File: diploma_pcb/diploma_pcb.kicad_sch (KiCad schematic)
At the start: 22 parts, among them Q1 2SC3356, Q3 2SC3356

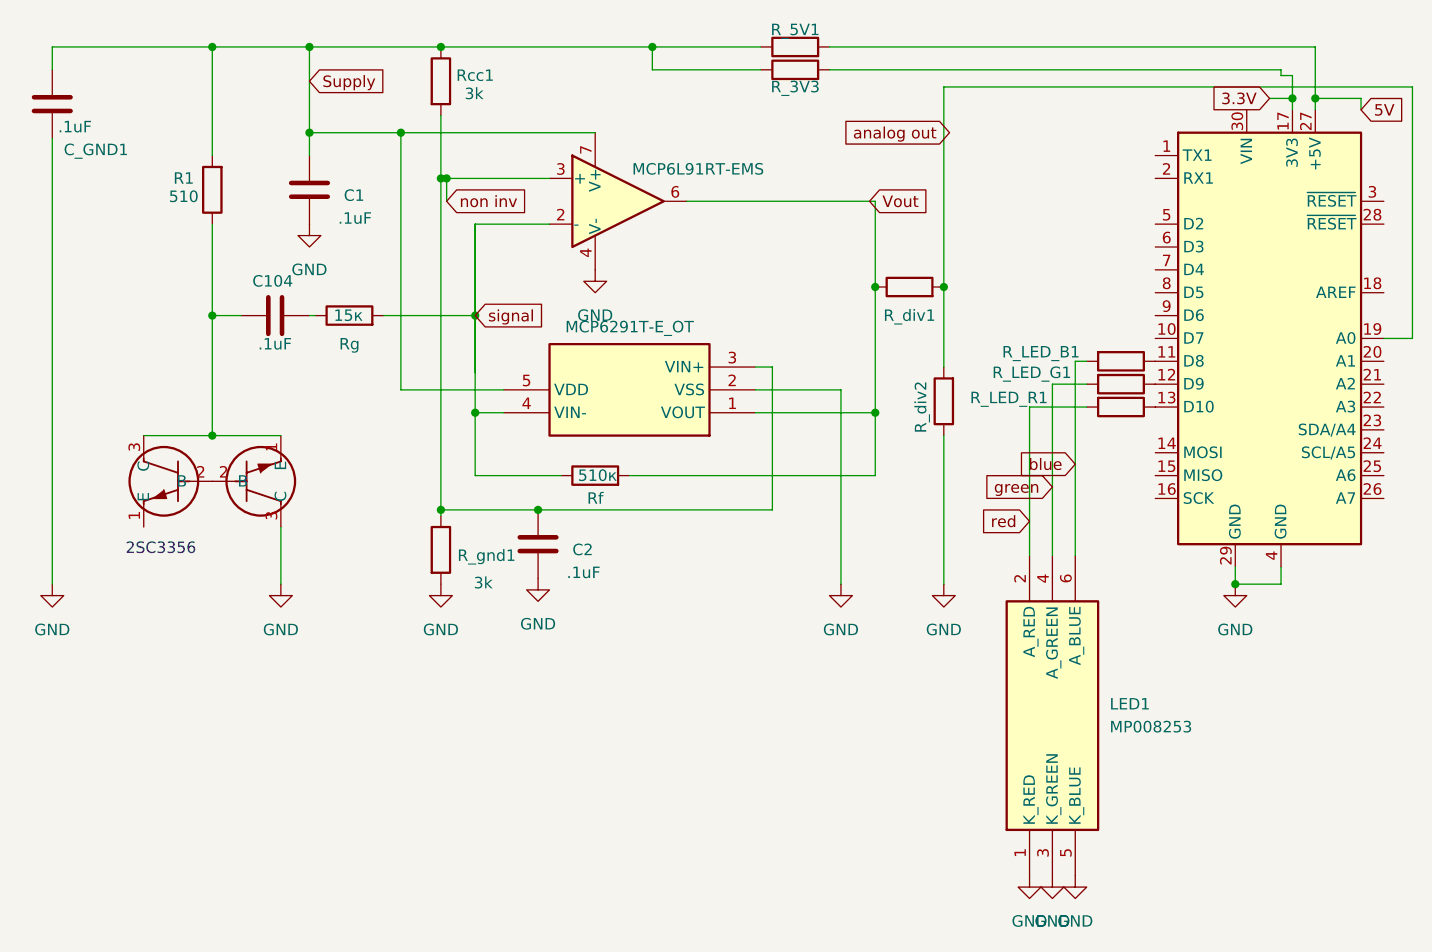
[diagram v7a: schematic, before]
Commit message: PCB added cap, larger pads, partialy fixed footprints
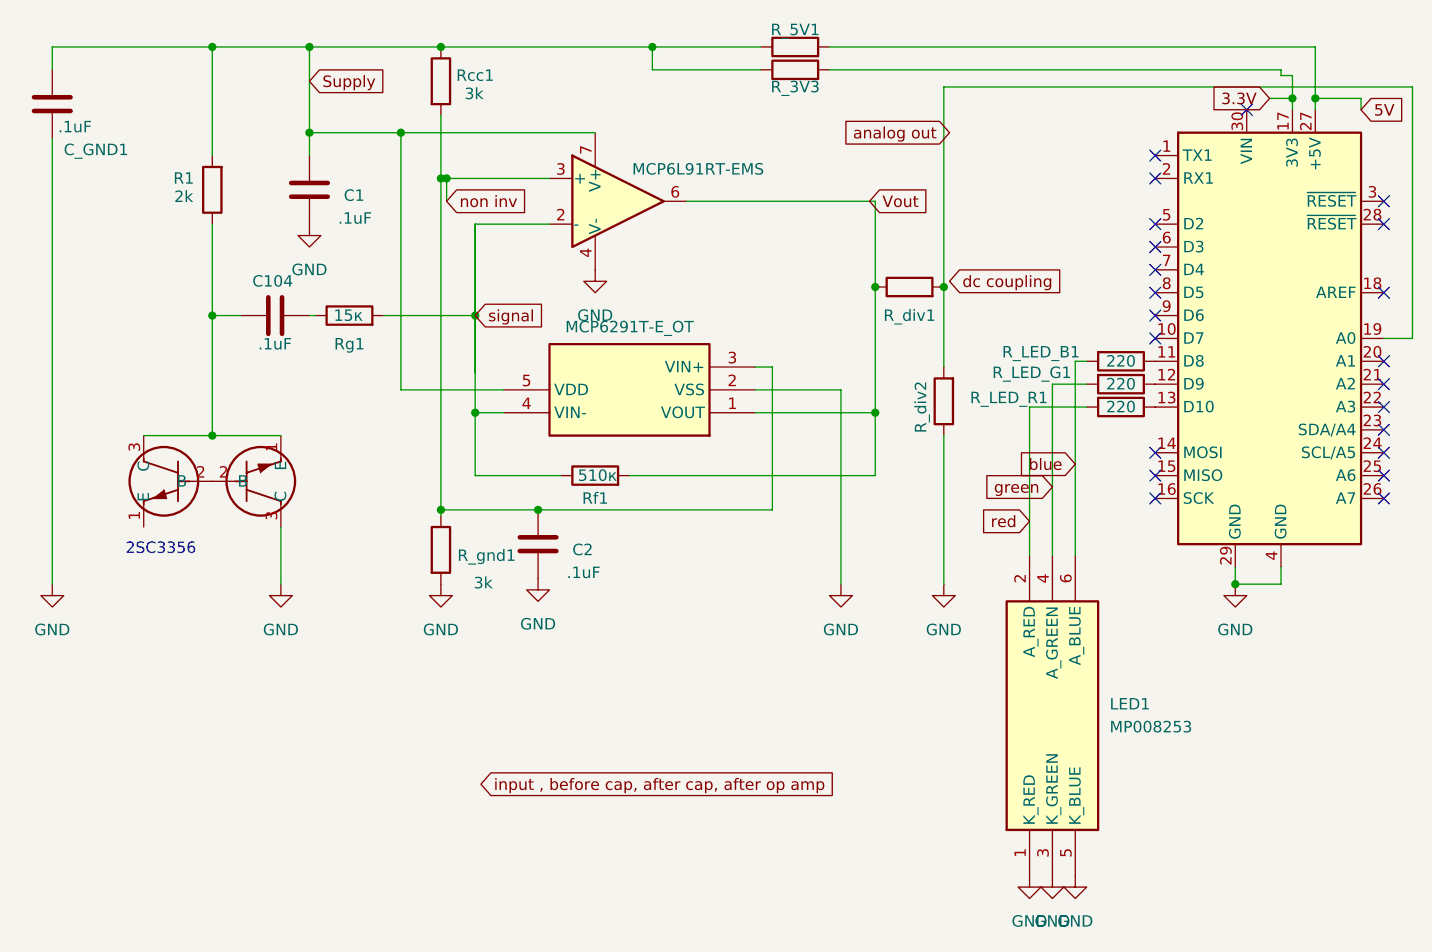
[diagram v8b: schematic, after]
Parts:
- R1: value 510 -> 2k
- R_LED_B1, R_LED_G1, R_LED_R1: value R -> 220
- renumbered Rf to Rf1, Rg to Rg1
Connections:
- no-connect marks 0 -> 22
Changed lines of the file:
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@@
 		(color 0 0 0 0)
 	)
+	(no_connect
+		(at 179.07 59.69)
+	)
+	(no_connect
+		(at 153.67 44.45)
+	)
+	(no_connect
+		(at 153.67 59.69)
+	)
+	(no_connect
+		(at 153.67 41.91)
+	)
+	(no_connect
+		(at 179.07 64.77)
+	)
+	(no_connect
+		(at 163.83 21.59)
+	)
+	(no_connect
+		(at 153.67 62.23)
+	)
+	(no_connect
+		(at 179.07 49.53)
+	)
+	(no_connect
+		(at 179.07 54.61)
+	)
+	(no_connect
+		(at 179.07 41.91)
+	)
+	(no_connect
+		(at 179.07 62.23)
+	)
+	(no_connect
+		(at 153.67 34.29)
+	)
+	(no_connect
+		(at 153.67 64.77)
+	)
+	(no_connect
+		(at 153.67 36.83)
+	)
+	(no_connect
+		(at 179.07 31.75)
+	)
+	(no_connect
+		(at 153.67 39.37)
+	)
+	(no_connect
+		(at 179.07 52.07)
+	)
+	(no_connect
+		(at 179.07 57.15)
+	)
+	(no_connect
+		(at 153.67 29.21)
+	)
+	(no_connect
+		(at 153.67 26.67)
+	)
+	(no_connect
+		(at 179.07 34.29)
+	)
+	(no_connect
+		(at 153.67 46.99)
+	)
 	(wire
 		(pts
@@
 		)
 	)
+	(global_label "input , before cap, after cap, after op amp"
+		(shape input)
+		(at 78.74 96.52 0)
+		(fields_autoplaced yes)
+		(effects
+			(font
+				(size 1.27 1.27)
+			)
+			(justify left)
+		)
+		(property "Intersheetrefs" "${INTERSHEET_REFS}"
+			(at 124.0579 96.52 0)
+			(effects
+				(font
+					(size 1.27 1.27)
+				)
+				(justify left)
+				(hide yes)
+			)
+		)
+	)
 	(global_label "red"
 		(shape input)
@@
 		)
 	)
+	(global_label "dc coupling"
+		(shape input)
+		(at 130.81 40.64 0)
+		(fields_autoplaced yes)
+		(effects
+			(font
+				(size 1.27 1.27)
+			)
+			(justify left)
+		)
+		(property "Intersheetrefs" "${INTERSHEET_REFS}"
+			(at 145.104 40.64 0)
+			(effects
+				(font
+					(size 1.27 1.27)
+				)
+				(justify left)
+				(hide yes)
+			)
+		)
+	)
 	(global_label "5V"
 		(shape input)
@@
 			)
 		)
-		(property "Value" "R"
-			(at 149.86 58.42 90)
+		(property "Value" "220"
+			(at 149.86 54.61 90)
 			(effects
 				(font
 					(size 1.27 1.27)
 				)
-				(hide yes)
 			)
 		)
@@
 		(on_board yes)
 		(dnp no)
-		(property "Reference" "Rf"
+		(property "Reference" "Rf1"
 			(at 91.44 64.77 90)
 			(effects
@@
 			(project "diploma_pcb"
 				(path "/8eade999-89f4-4618-aeea-e9238b0bd165"
-					(reference "Rf")
+					(reference "Rf1")
 					(unit 1)
 				)
@@
 			)
 		)
-		(property "Value" "R"
-			(at 149.86 55.88 90)
+		(property "Value" "220"
+			(at 149.86 52.07 90)
 			(effects
 				(font
 					(size 1.27 1.27)
 				)
-				(hide yes)
 			)
 		)
@@
 			)
 		)
-		(property "Value" "R"
-			(at 149.86 53.34 90)
+		(property "Value" "220"
+			(at 149.86 49.53 90)
 			(effects
 				(font
 					(size 1.27 1.27)
 				)
-				(hide yes)
 			)
 		)
@@
 		(on_board yes)
 		(dnp no)
-		(property "Reference" "Rg"
+		(property "Reference" "Rg1"
 			(at 64.135 47.625 90)
 			(effects
@@
 			(project "diploma_pcb"
 				(path "/8eade999-89f4-4618-aeea-e9238b0bd165"
-					(reference "Rg")
+					(reference "Rg1")
 					(unit 1)
 				)
@@
 			)
 		)
-		(property "Value" "510"
+		(property "Value" "2k"
 			(at 45.72 31.242 0)
 			(effects
